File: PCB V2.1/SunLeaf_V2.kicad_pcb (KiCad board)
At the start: 4 copper layers, 80 x 40 mm, 107 parts, among them IC1 ESP_09, J1 20021121-00010C4LF, J10 B4B-PH-K-S(LF)(SN), J11 B4B-PH-K-S(LF)(SN), J12 B4B-PH-K-S(LF)(SN), J13 B4B-PH-K-S(LF)(SN), J14 B4B-PH-K-S(LF)(SN), J15 B4B-PH-K-S(LF)(SN), J16 B4B-PH-K-S(LF)(SN), J2 0475890001-MicroUSBPort, J3 B2B-PH-K-S(LF)(SN), J4 B3B-PH-K-S(LF)(SN), J5 B4B-PH-K-S(LF)(SN), J6 B4B-PH-K-S(LF)(SN), J7 B4B-PH-K-S(LF)(SN), J8 B4B-PH-K-S(LF)(SN), J9 B4B-PH-K-S(LF)(SN), P1 CONN_01X04, Q1 DMG2307L-7, Q2 DMG2307L-7, SW1 B3U-1000P, SW2 B3U-1000P, T1 1909763-1, U1 STM32F446RET6_-_TQFP64, U2 BQ24210DQCT, U3 AZ1117CR-3.3TRG1_1, U4 74HC4052D, U5 PCA9518DBQR, X1 ABM3B8.000MHZB2T, X2 ABS07-32.768KHZ-9-T

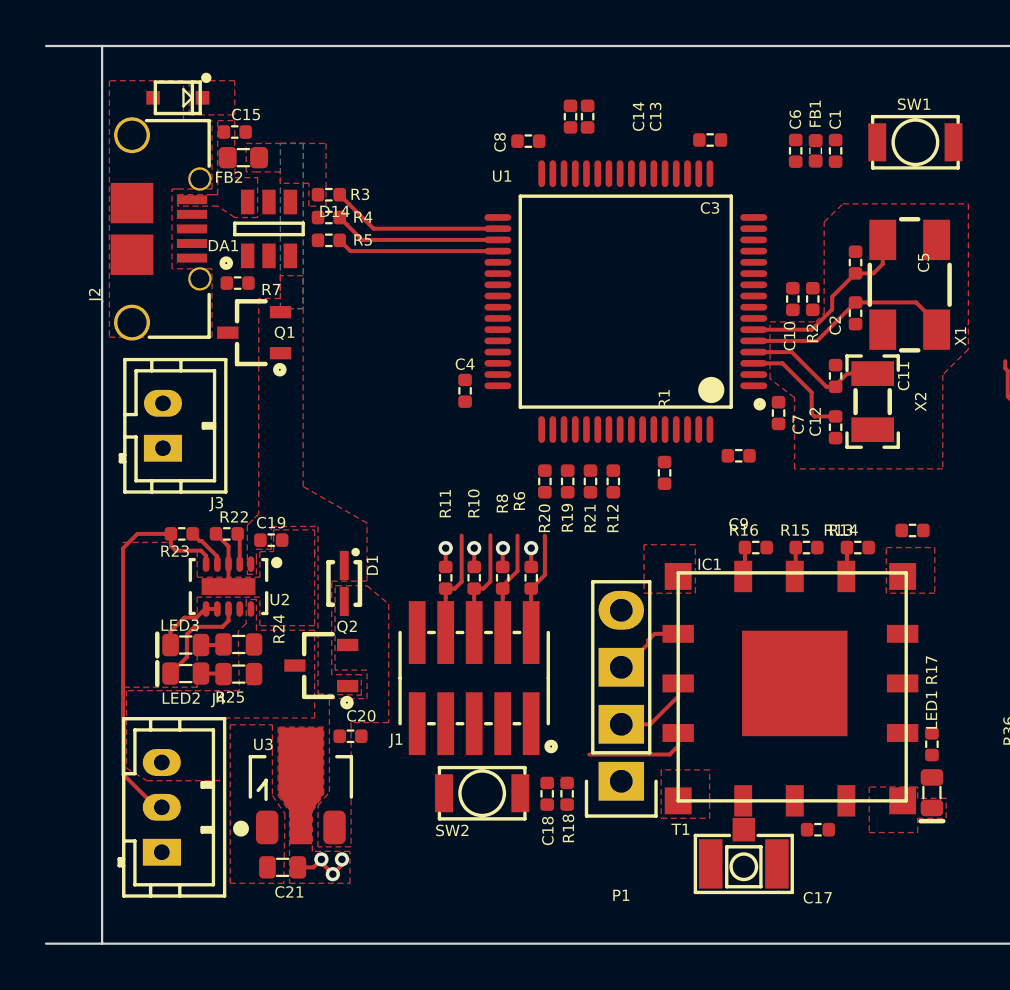
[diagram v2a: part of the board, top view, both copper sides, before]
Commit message: Routing and Placement
Placement complete routing has begun. The board size has also been
solidified.
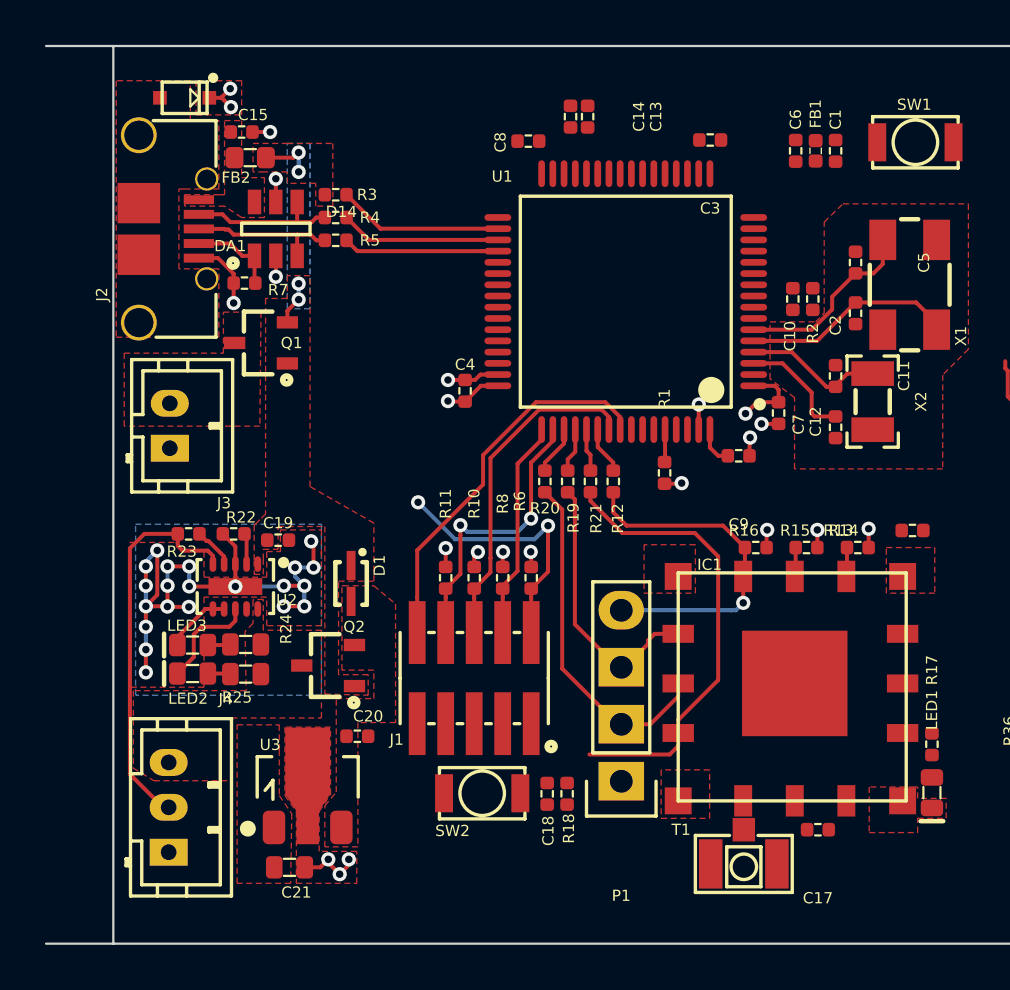
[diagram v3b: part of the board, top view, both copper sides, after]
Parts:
- moved Q1 0.55 mm to (49.6, 43.2)
- moved C15 0.30 mm to (48.7, 33.8)
- moved C19 0.30 mm to (50.3, 52.0)
- moved C20 0.30 mm to (53.9, 60.8)
- moved C21 0.30 mm to (50.9, 66.6)
- moved D1 0.30 mm to (53.6, 53.9)
- moved D14 0.30 mm to (46.2, 32.3)
- moved DA1 0.30 mm to (50.2, 38.2)
- moved FB2 0.30 mm to (49.1, 35.0)
- moved J2 0.30 mm to (46.8, 38.2)
- moved J3 0.30 mm to (45.5, 47.9)
- moved J4 0.30 mm to (45.5, 65.9)
- moved LED2 0.30 mm to (46.5, 58.0)
- moved LED3 0.30 mm to (46.5, 56.7)
- moved Q2 0.30 mm to (52.6, 57.6)
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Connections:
- U1 pad 55: /MCU-STM32F446RET6/SWO_TDI -> /MCU-STM32F446RET6/SWO_TDO
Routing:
- net GND: track 2.58 -> 40.8 mm, vias 0 -> 33
- net /MCU-STM32F446RET6/NJTRST: track 0.00 -> 17.0 mm
- net Net-(C18-Pad1): track 4.69 -> 20.4 mm
- net /WiFi-ESP8266-ESP-09/PGM_MODE: track 1.32 -> 15.5 mm, vias 0 -> 1
- net Net-(IC1-Pad11): track 3.63 -> 15.5 mm
- net /MCU-STM32F446RET6/SWO_TDO: track 4.87 -> 14.9 mm
- net Net-(IC1-Pad10): track 3.24 -> 12.1 mm
- net +3V3: track 6.25 -> 15.1 mm, vias 7 -> 11
- net /MCU-STM32F446RET6/SWO_TDI: track 4.85 -> 12.9 mm, vias 0 -> 2
- net /MCU-STM32F446RET6/SWDIO_TMS: track 4.57 -> 11.8 mm, vias 0 -> 2
- net Net-(DA1-Pad3): track 0.00 -> 6.78 mm
- net Net-(DA1-Pad4): track 0.00 -> 6.74 mm
- net /MCU-STM32F446RET6/SWCLK_TCK: track 4.59 -> 9.76 mm
- net /MCU-STM32F446RET6/VBUS: track 0.00 -> 4.35 mm, vias 0 -> 4
- net Net-(DA1-Pad1): track 0.00 -> 3.93 mm
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- added copper zone on B.Cu, net GND
- added copper zone on F.Cu, net Net-(J3-Pad2)
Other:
- outline, holes or cut-outs redrawn

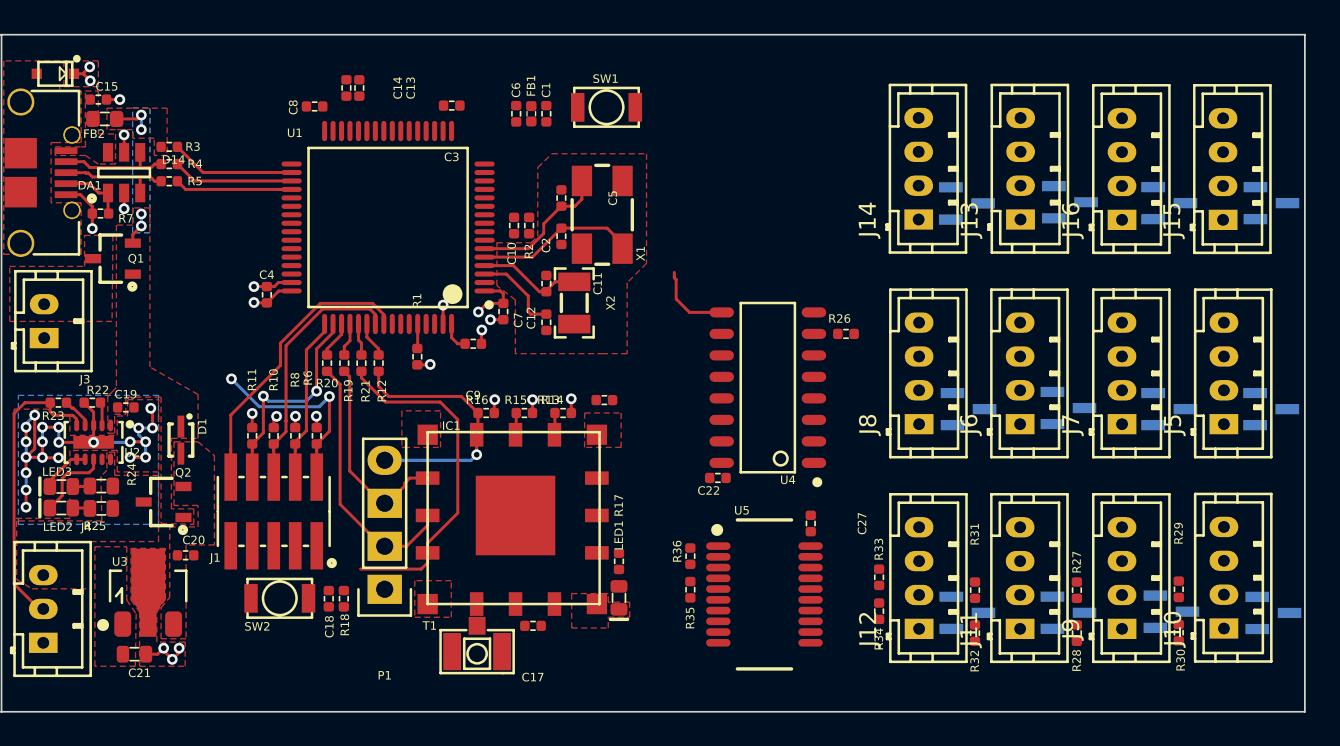
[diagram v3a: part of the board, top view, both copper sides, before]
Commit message: Routing Progress
Routing progress made, UART and I2C sensors routed, ESP routed, power
section and solar batter routed, USB routed.
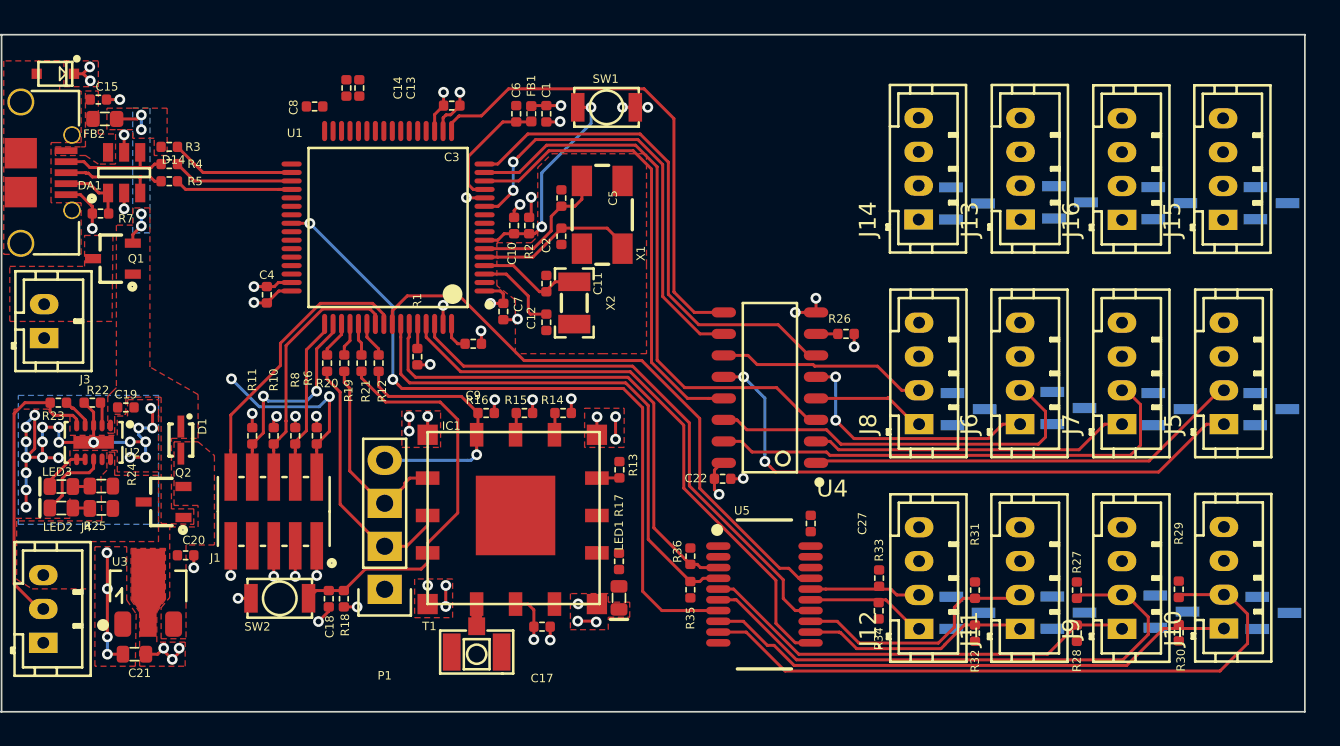
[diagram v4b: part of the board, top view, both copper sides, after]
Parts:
- moved R13 4.21 mm to (79.5, 55.7), turned to 270 degrees
- moved C17 0.54 mm to (74.9, 65.0)
- moved C22 0.28 mm to (85.6, 56.2), turned to 0 degrees
- moved U4 0.12 mm to (88.4, 50.9)
- moved R33 0.05 mm to (94.8, 62.1)
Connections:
- J1 pad 3: Net-(J1-Pad3) -> GND
- J1 pad 5: Net-(J1-Pad3) -> GND
- J1 pad 9: Net-(J1-Pad3) -> GND
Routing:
- net /I2C Grove Sensors/EN1_IMUX: track 0.00 -> 43.6 mm, vias 0 -> 2
- net Net-(D7-Pad2): track 0.00 -> 39.2 mm
- net /UART Grove Sensors/UART_RX0: track 0.00 -> 35.4 mm, vias 0 -> 2
- net /I2C Grove Sensors/EN4_IMUX: track 0.00 -> 35.2 mm
- net /I2C Grove Sensors/EN2_IMUX: track 0.00 -> 34.6 mm
- net /MCU-STM32F446RET6/UART_S_RX: track 0.00 -> 33.7 mm
- net Net-(D6-Pad2): track 0.00 -> 33.4 mm
- net /I2C Grove Sensors/EN3_IMUX: track 0.00 -> 32.5 mm
- net Net-(D7-Pad1): track 0.00 -> 31.9 mm
- net /I2C Grove Sensors/I2C_SCL: track 0.00 -> 31.5 mm
- net GND: track 40.8 -> 71.6 mm, vias 33 -> 58
- net /MCU-STM32F446RET6/USW_EN: track 0.00 -> 30.3 mm
- net /I2C Grove Sensors/I2C_SDA: track 0.00 -> 30.2 mm
- net /UART Grove Sensors/UART_TX2: track 0.00 -> 29.2 mm
- net /UART Grove Sensors/UART_S_RX: track 0.00 -> 27.6 mm
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
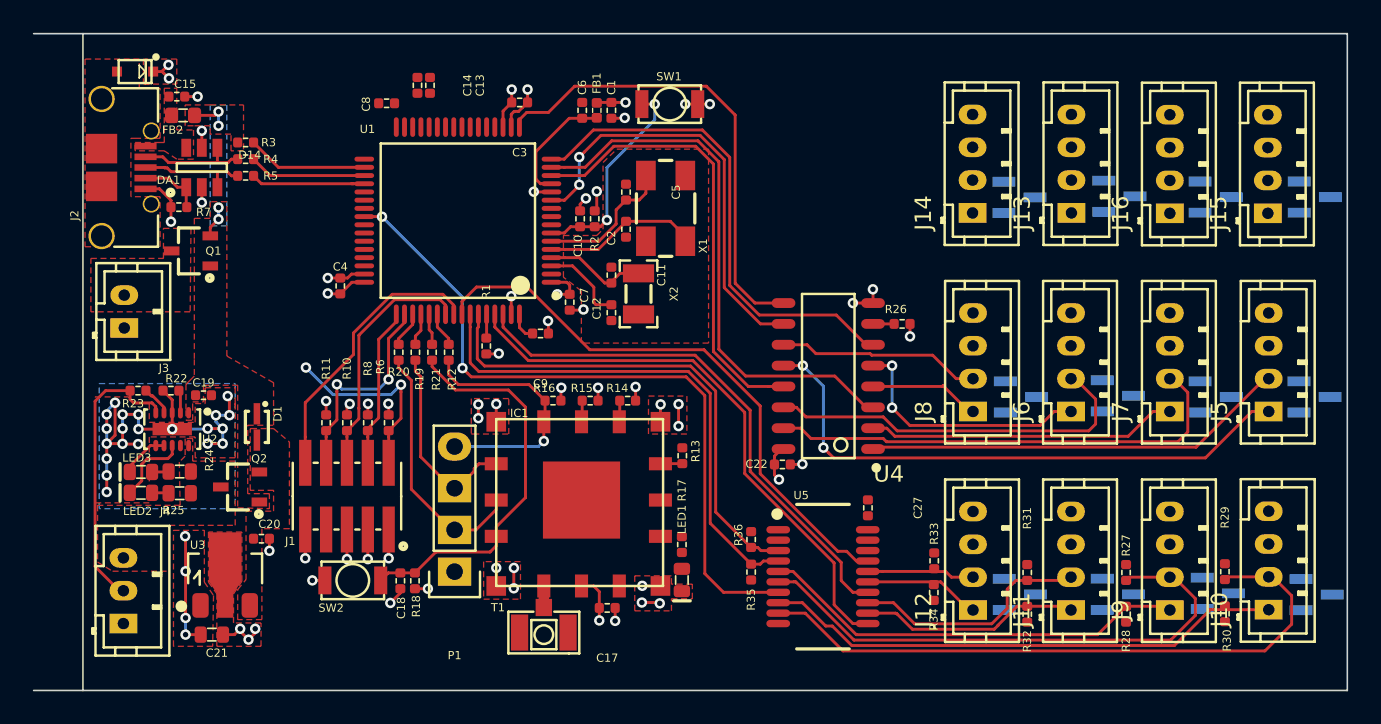
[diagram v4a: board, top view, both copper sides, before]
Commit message: Route 99%
PCB routing at 99%, next commit complete route and internal layers.
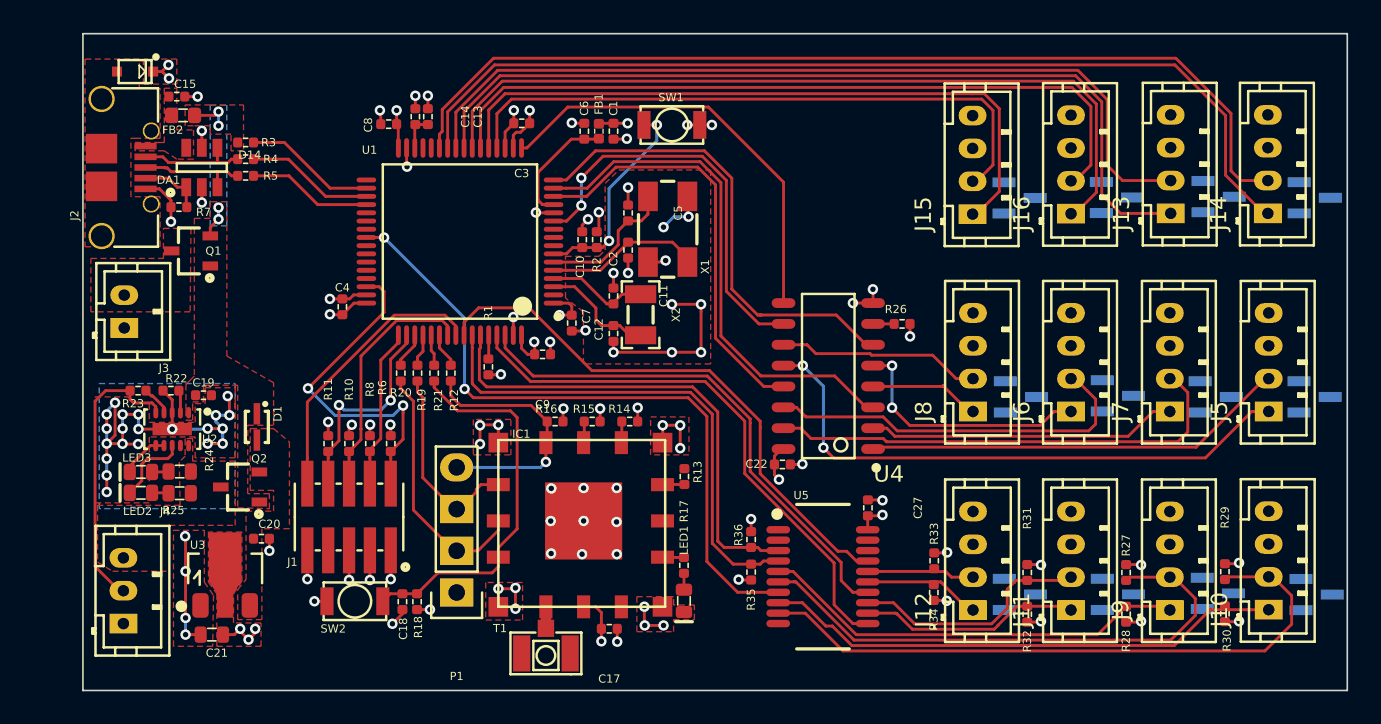
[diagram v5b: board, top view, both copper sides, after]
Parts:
- moved D11 18.0 mm to (100.0, 40.0)
- moved J15 18.0 mm to (97.2, 41.0)
- moved D12 18.0 mm to (118.0, 40.0)
- moved J14 18.0 mm to (115.2, 40.9)
- moved J13 6.05 mm to (109.2, 40.9)
- moved D13 6.05 mm to (112.2, 39.9)
- moved D10 6.02 mm to (106.0, 40.0)
- moved J16 6.02 mm to (103.2, 41.0)
- moved C13 1.91 mm to (64.0, 35.1)
- moved C14 1.91 mm to (63.2, 35.1)
- moved C1 1.28 mm to (75.3, 35.9)
- moved C10 1.28 mm to (73.4, 42.5)
- moved C2 1.28 mm to (76.2, 43.2)
- moved IC1 1.28 mm to (68.3, 64.9)
- moved R1 1.28 mm to (67.7, 50.3)
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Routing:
- net /Analog and Digital Grove IO/ANIO_3: track 0.00 -> 59.2 mm
- net /Analog and Digital Grove IO/ANIO_2: track 0.00 -> 59.1 mm
- net /Analog and Digital Grove IO/ANIO_1: track 0.00 -> 52.9 mm
- net /Analog and Digital Grove IO/ANIO_0: track 0.00 -> 52.4 mm
- net /Analog and Digital Grove IO/ANIO_7: track 0.00 -> 49.0 mm
- net GND: track 71.6 -> 120.2 mm, vias 58 -> 92
- net /Analog and Digital Grove IO/ANIO_6: track 0.00 -> 46.0 mm
- net /Analog and Digital Grove IO/ANIO_5: track 0.00 -> 41.6 mm
- net /Analog and Digital Grove IO/ANIO_4: track 0.00 -> 38.0 mm
- net +3V3: track 27.4 -> 40.7 mm, vias 18 -> 31
- net /MCU-STM32F446RET6/SWDIO_TMS: track 11.8 -> 20.8 mm
- net (no net): track 4.60 -> 0.00 mm, vias 8 -> 0
- net /MCU-STM32F446RET6/USW_S1: track 28.8 -> 26.2 mm
- net Net-(C13-Pad1): track 0.00 -> 2.20 mm
- net /MCU-STM32F446RET6/UART_S_RX: track 33.7 -> 31.8 mm
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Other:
- board size 80 x 40 mm -> 77 x 40 mm
